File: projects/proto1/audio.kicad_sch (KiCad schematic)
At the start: 26 parts, among them J14 AUDIO_DATA, J15 STX-4335-5BGP-S1, U51 CS4231A, Y2 16.9344M, Y3 24.576M

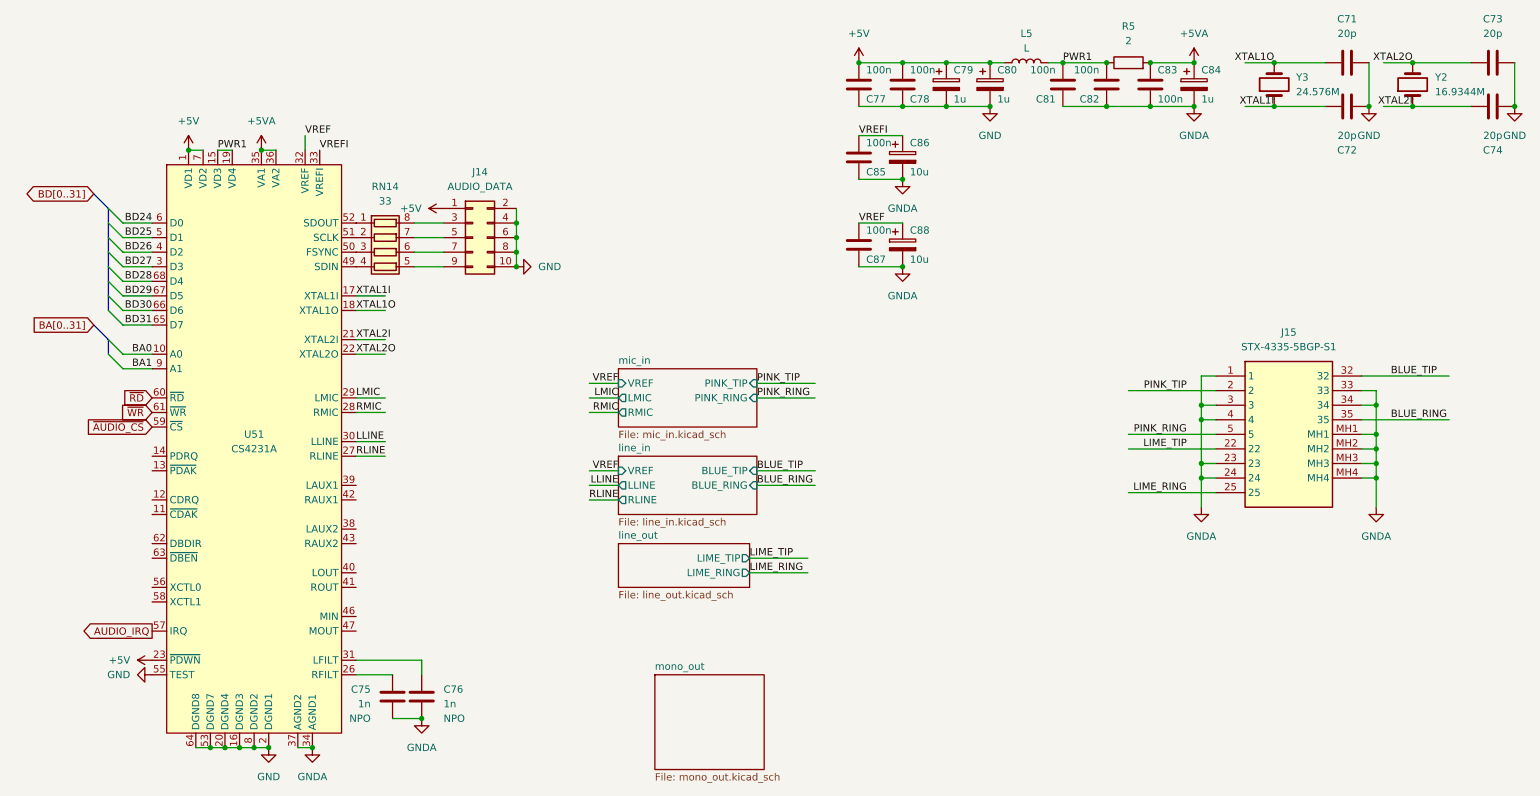
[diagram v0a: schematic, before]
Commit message: Renamed CMC to SCU, changed verification method to cocotb, and modified pcb schematic
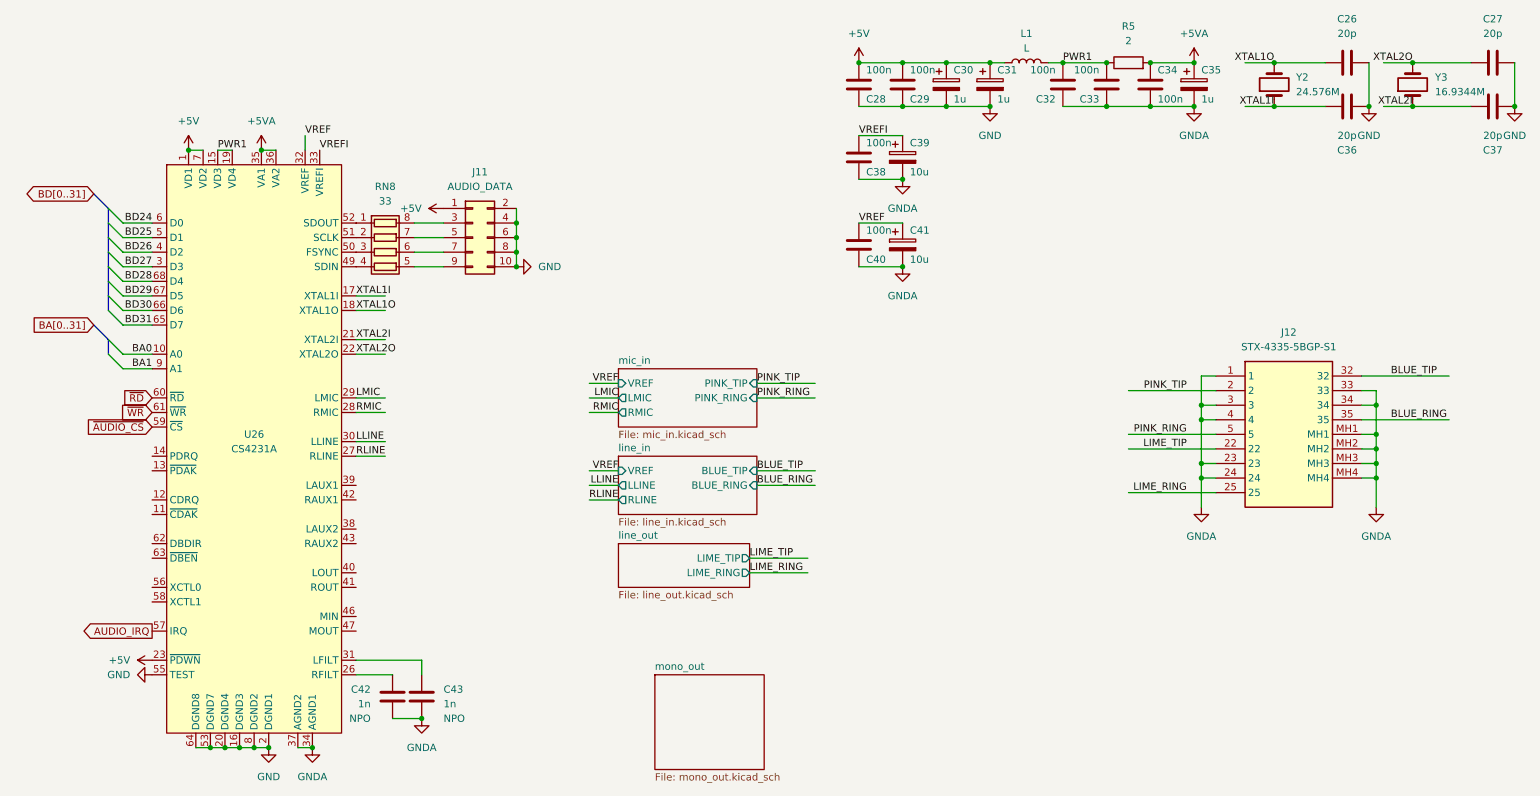
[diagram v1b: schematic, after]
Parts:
- renumbered C71 to C26, C73 to C27, C77 to C28, C78 to C29, C79 to C30, C80 to C31, C81 to C32, C82 to C33, C83 to C34, C84 to C35, C72 to C36, C74 to C37, C85 to C38, C86 to C39, C87 to C40, C88 to C41, C75 to C42, C76 to C43, J14 to J11, J15 to J12, L5 to L1, RN14 to RN8, U51 to U26, Y3 to Y2, Y2 to Y3
